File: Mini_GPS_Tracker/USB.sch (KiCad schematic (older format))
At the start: 3 parts, among them J5 USB_B_Micro, U11 FT230XS

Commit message: Add files via upload
Breaking out more pins
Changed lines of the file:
@@
 	4650 5600 4650 5450
 Connection ~ 4550 5600
-Text GLabel 5400 4550 2    50   Input ~ 0
-RTS
 Wire Wire Line
 	5250 4550 5400 4550
-Text GLabel 5600 4450 2    50   Input ~ 0
-USB_RX
-Text GLabel 5600 4350 2    50   Input ~ 0
-USB_TX
 Wire Wire Line
 	5250 4350 5600 4350
@@
 Wire Wire Line
 	1950 5100 2050 5100
-Text GLabel 2950 4450 2    50   Input ~ 0
-VBUS
 Wire Wire Line
 	2850 3750 2850 4450
@@
 Wire Wire Line
 	2550 4750 2350 4750
+Text HLabel 5600 4350 2    50   Input ~ 0
+USB_TX
+Text HLabel 5600 4450 2    50   Input ~ 0
+USB_RX
+Text HLabel 5400 4550 2    50   Input ~ 0
+RTS
+Text HLabel 2950 4450 2    50   Input ~ 0
+VBUS
 $EndSCHEMATC

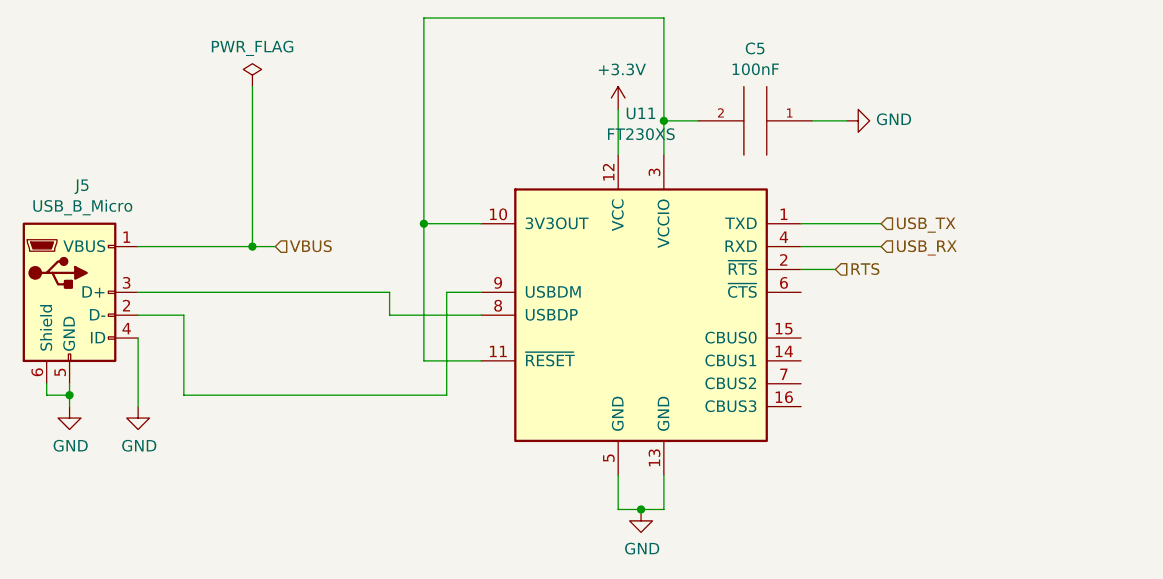
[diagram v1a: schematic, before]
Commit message: Add files via upload
More changes - USB, WiFi/BT, Buzzer, Siren-LED Flasher
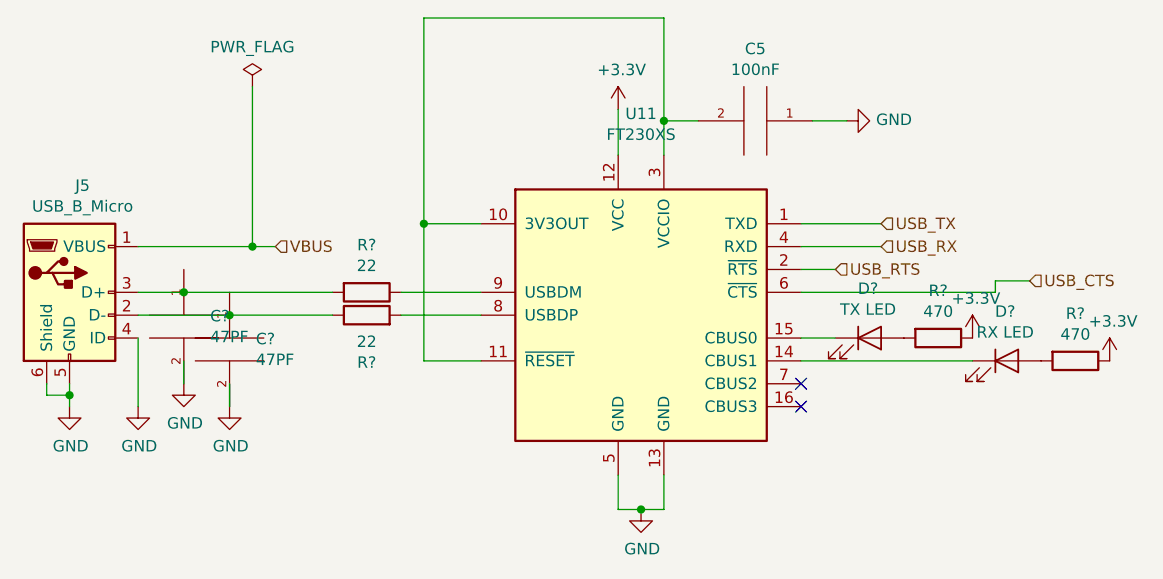
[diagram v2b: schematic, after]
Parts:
- added C? (x2): 47PF, symbol Device:C
- added D?: TX LED, symbol Device:LED
- added D?: RX LED, symbol Device:LED
- added R? (x2): 22, symbol Device:R
- added R? (x2): 470, symbol Device:R
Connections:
- net labels added: USB_CTS, USB_RTS
- net labels removed: RTS
- wire segments 33 -> 38
- no-connect marks 0 -> 2
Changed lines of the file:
@@
 Wire Wire Line
 	2350 4850 2350 5150
-Wire Wire Line
-	2350 4650 3450 4650
-Wire Wire Line
-	3450 4650 3450 4750
-Wire Wire Line
-	3450 4750 3850 4750
-Wire Wire Line
-	3850 4650 3700 4650
-Wire Wire Line
-	3700 4650 3700 5100
-Wire Wire Line
-	3700 5100 2550 5100
-Wire Wire Line
-	2550 5100 2550 4750
-Wire Wire Line
-	2550 4750 2350 4750
 Text HLabel 5600 4350 2    50   Input ~ 0
 USB_TX
@@
 USB_RX
 Text HLabel 5400 4550 2    50   Input ~ 0
-RTS
+USB_RTS
 Text HLabel 2950 4450 2    50   Input ~ 0
 VBUS
+$Comp
+L Device:R R?
+U 1 1 5EB878AE
+P 3350 4650
+F 0 "R?" V 3143 4650 50  0000 C CNN
+F 1 "22" V 3234 4650 50  0000 C CNN
+F 2 "" V 3280 4650 50  0001 C CNN
+F 3 "~" H 3350 4650 50  0001 C CNN
+	1    3350 4650
+	0    1    1    0
+$EndComp
+$Comp
+L Device:R R?
+U 1 1 5EB87E49
+P 3350 4750
+F 0 "R?" V 3143 4750 50  0000 C CNN
+F 1 "22" V 3234 4750 50  0000 C CNN
+F 2 "" V 3280 4750 50  0001 C CNN
+F 3 "~" H 3350 4750 50  0001 C CNN
+	1    3350 4750
+	0    -1   -1   0
+$EndComp
+Wire Wire Line
+	3500 4650 3850 4650
+Wire Wire Line
+	3500 4750 3850 4750
+Wire Wire Line
+	2350 4650 2550 4650
+Wire Wire Line
+	2350 4750 2750 4750
+$Comp
+L Device:LED D?
+U 1 1 5EB896A2
+P 5550 4850
+F 0 "D?" H 5543 5066 50  0000 C CNN
+F 1 "TX LED" H 5543 4975 50  0000 C CNN
+F 2 "" H 5550 4850 50  0001 C CNN
+F 3 "~" H 5550 4850 50  0001 C CNN
+	1    5550 4850
+	1    0    0    -1
+$EndComp
+Wire Wire Line
+	5250 4850 5400 4850
+$Comp
+L Device:R R?
+U 1 1 5EB8A40C
+P 5850 4850
+F 0 "R?" V 5643 4850 50  0000 C CNN
+F 1 "470" V 5734 4850 50  0000 C CNN
+F 2 "" V 5780 4850 50  0001 C CNN
+F 3 "~" H 5850 4850 50  0001 C CNN
+	1    5850 4850
+	0    1    1    0
+$EndComp
+$Comp
+L power:+3.3V #PWR?
+U 1 1 5EB8A988
+P 6000 4850
+F 0 "#PWR?" H 6000 4700 50  0001 C CNN
+F 1 "+3.3V" H 6015 5023 50  0000 C CNN
+F 2 "" H 6000 4850 50  0001 C CNN
+F 3 "" H 6000 4850 50  0001 C CNN
+	1    6000 4850
+	1    0    0    -1
+$EndComp
+$Comp
+L Device:LED D?
+U 1 1 5EB8C1BC
+P 6150 4950
+F 0 "D?" H 6143 5166 50  0000 C CNN
+F 1 "RX LED" H 6143 5075 50  0000 C CNN
+F 2 "" H 6150 4950 50  0001 C CNN
+F 3 "~" H 6150 4950 50  0001 C CNN
+	1    6150 4950
+	1    0    0    -1
+$EndComp
+$Comp
+L Device:R R?
+U 1 1 5EB8C1C3
+P 6450 4950
+F 0 "R?" V 6243 4950 50  0000 C CNN
+F 1 "470" V 6334 4950 50  0000 C CNN
+F 2 "" V 6380 4950 50  0001 C CNN
+F 3 "~" H 6450 4950 50  0001 C CNN
+	1    6450 4950
+	0    1    1    0
+$EndComp
+$Comp
+L power:+3.3V #PWR?
+U 1 1 5EB8C1C9
+P 6600 4950
+F 0 "#PWR?" H 6600 4800 50  0001 C CNN
+F 1 "+3.3V" H 6615 5123 50  0000 C CNN
+F 2 "" H 6600 4950 50  0001 C CNN
+F 3 "" H 6600 4950 50  0001 C CNN
+	1    6600 4950
+	1    0    0    -1
+$EndComp
+Wire Wire Line
+	5250 4950 6000 4950
+NoConn ~ 5250 5050
+NoConn ~ 5250 5150
+$Comp
+L Device:C C?
+U 1 1 5EB8D7F2
+P 2750 4900
+F 0 "C?" H 2865 4946 50  0000 L CNN
+F 1 "47PF" H 2865 4855 50  0000 L CNN
+F 2 "" H 2788 4750 50  0001 C CNN
+F 3 "~" H 2750 4900 50  0001 C CNN
+	1    2750 4900
+	1    0    0    -1
+$EndComp
+Connection ~ 2750 4750
+Wire Wire Line
+	2750 4750 3200 4750
+$Comp
+L power:GND #PWR?
+U 1 1 5EB8DD14
+P 2750 5150
+F 0 "#PWR?" H 2750 4900 50  0001 C CNN
+F 1 "GND" H 2755 4977 50  0000 C CNN
+F 2 "" H 2750 5150 50  0001 C CNN
+F 3 "" H 2750 5150 50  0001 C CNN
+	1    2750 5150
+	1    0    0    -1
+$EndComp
+Wire Wire Line
+	2750 5050 2750 5150
+$Comp
+L Device:C C?
+U 1 1 5EB90331
+P 2550 4800
+F 0 "C?" H 2665 4846 50  0000 L CNN
+F 1 "47PF" H 2665 4755 50  0000 L CNN
+F 2 "" H 2588 4650 50  0001 C CNN
+F 3 "~" H 2550 4800 50  0001 C CNN
+	1    2550 4800
+	1    0    0    -1
+$EndComp
+$Comp
+L power:GND #PWR?
+U 1 1 5EB90337
+P 2550 5050
+F 0 "#PWR?" H 2550 4800 50  0001 C CNN
+F 1 "GND" H 2555 4877 50  0000 C CNN
+F 2 "" H 2550 5050 50  0001 C CNN
+F 3 "" H 2550 5050 50  0001 C CNN
+	1    2550 5050
+	1    0    0    -1
+$EndComp
+Wire Wire Line
+	2550 4950 2550 5050
+Connection ~ 2550 4650
+Wire Wire Line
+	2550 4650 3200 4650
+Wire Wire Line
+	6100 4600 6250 4600
+Text HLabel 6250 4600 2    50   Input ~ 0
+USB_CTS
+Wire Wire Line
+	5250 4650 6100 4650
+Wire Wire Line
+	6100 4650 6100 4600
 $EndSCHEMATC
